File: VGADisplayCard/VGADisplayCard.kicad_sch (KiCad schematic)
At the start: 3 parts, among them J2 Bus_PCI_Express_x1

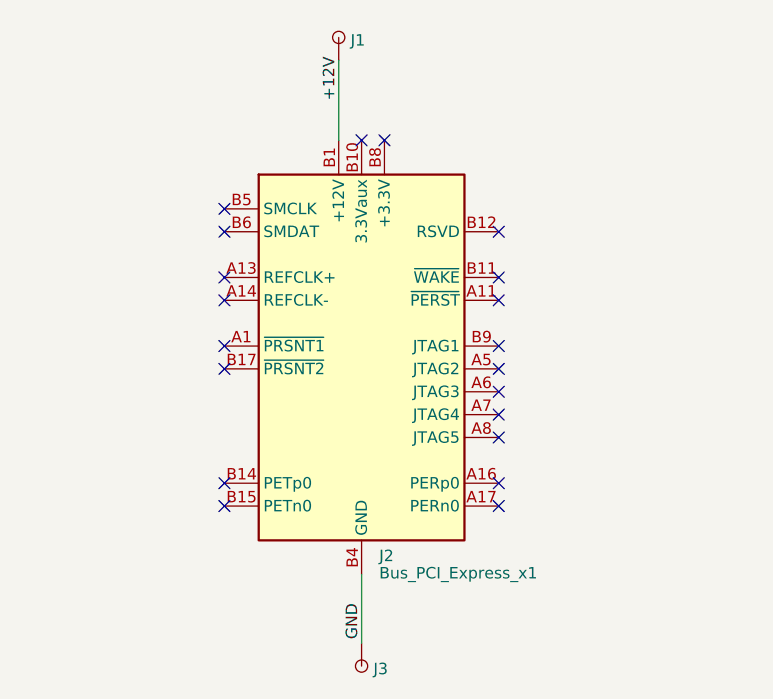
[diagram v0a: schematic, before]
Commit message: vga mount polish and 2.54mm mount (closes #37)
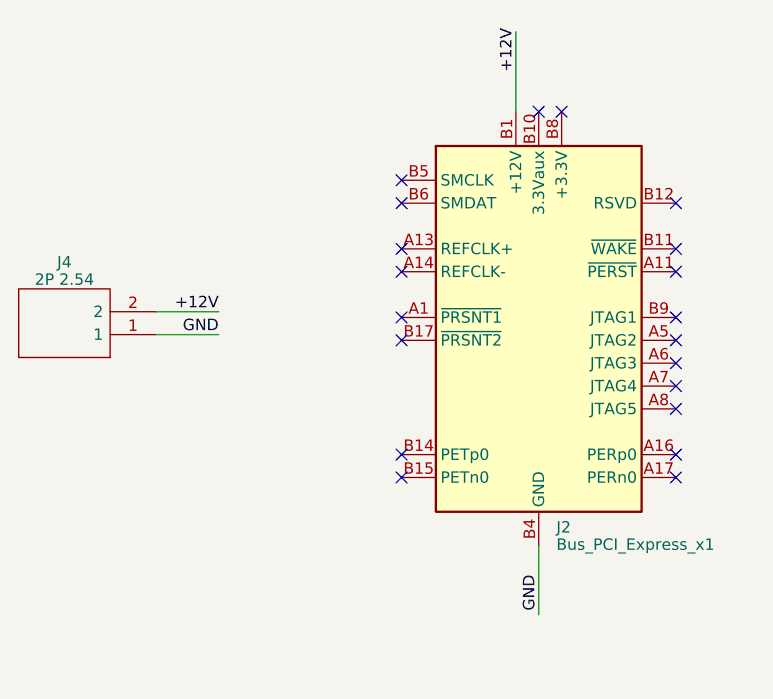
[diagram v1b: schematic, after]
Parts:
- removed J1, J3: ~, Oro Footprints:DebugPin, symbol Oro:DebugPin
- added J4: 2P 2.54, HDRV2W67P0X254_1X2_508X241X1082P, symbol SamacSys_Parts:10129378-902003BLF
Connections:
- net +12V: now also J4.2
- net GND: now also J4.1
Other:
- moved on the sheet: J2
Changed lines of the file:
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@@
   (title_block
     (title "PCIe.1x 12v Supply + VGA Mount")
-    (date "2023-06-09")
-    (rev "1")
+    (date "2023-07-02")
+    (rev "2")
     (company "Oro Operating System")
     (comment 1 "://oro.sh")
     (comment 2 "Joshua Lee Junon")
   )
-  (no_connect (at 158.115 106.045))
-  (no_connect (at 158.115 88.265))
-  (no_connect (at 158.115 108.585))
-  (no_connect (at 158.115 118.745))
-  (no_connect (at 142.875 78.105))
-  (no_connect (at 158.115 111.125))
-  (no_connect (at 158.115 95.885))
-  (no_connect (at 127.635 100.965))
-  (no_connect (at 127.635 116.205))
-  (no_connect (at 127.635 95.885))
-  (no_connect (at 158.115 116.205))
-  (no_connect (at 145.415 78.105))
-  (no_connect (at 158.115 100.965))
-  (no_connect (at 158.115 103.505))
-  (no_connect (at 127.635 103.505))
-  (no_connect (at 127.635 93.345))
-  (no_connect (at 127.635 88.265))
-  (no_connect (at 158.115 93.345))
-  (no_connect (at 127.635 118.745))
-  (no_connect (at 127.635 85.725))
-  (wire (pts (xy 142.875 126.365) (xy 142.875 133.985))
+  (no_connect (at 177.8 102.87))
+  (no_connect (at 177.8 85.09))
+  (no_connect (at 177.8 105.41))
+  (no_connect (at 177.8 115.57))
+  (no_connect (at 162.56 74.93))
+  (no_connect (at 177.8 107.95))
+  (no_connect (at 177.8 92.71))
+  (no_connect (at 147.32 97.79))
+  (no_connect (at 147.32 113.03))
+  (no_connect (at 147.32 92.71))
+  (no_connect (at 177.8 113.03))
+  (no_connect (at 165.1 74.93))
+  (no_connect (at 177.8 97.79))
+  (no_connect (at 177.8 100.33))
+  (no_connect (at 147.32 100.33))
+  (no_connect (at 147.32 90.17))
+  (no_connect (at 147.32 85.09))
+  (no_connect (at 177.8 90.17))
+  (no_connect (at 147.32 115.57))
+  (no_connect (at 147.32 82.55))
+  (wire (pts (xy 120.015 99.695) (xy 127 99.695))
     (stroke (width 0) (type default))
   )
-  (wire (pts (xy 140.335 69.215) (xy 140.335 78.105))
+  (wire (pts (xy 162.56 123.19) (xy 162.56 130.81))
     (stroke (width 0) (type default))
   )
-  (label "GND" (at 142.875 129.54 270) (fields_autoplaced)
+  (wire (pts (xy 120.015 97.155) (xy 127 97.155))
+    (stroke (width 0) (type default))
+  )
+  (wire (pts (xy 160.02 66.04) (xy 160.02 74.93))
+    (stroke (width 0) (type default))
+  )
+  (label "GND" (at 162.56 126.365 270) (fields_autoplaced)
     (effects (font (size 1.27 1.27)) (justify right bottom))
   )
-  (label "+12V" (at 140.335 73.66 90) (fields_autoplaced)
+  (label "+12V" (at 127 97.155 180) (fields_autoplaced)
+    (effects (font (size 1.27 1.27)) (justify right bottom))
+  )
+  (label "GND" (at 127 99.695 180) (fields_autoplaced)
+    (effects (font (size 1.27 1.27)) (justify right bottom))
+  )
+  (label "+12V" (at 160.02 70.485 90) (fields_autoplaced)
     (effects (font (size 1.27 1.27)) (justify left bottom))
   )
-  (symbol (lib_id "Connector:Bus_PCI_Express_x1") (at 142.875 103.505 0) (unit 1)
+  (symbol (lib_id "Connector:Bus_PCI_Express_x1") (at 162.56 100.33 0) (unit 1)
     (in_bom yes) (on_board yes) (dnp no) (fields_autoplaced)
-    (property "Reference" "J2" (at 144.8309 124.2775 0)
+    (property "Reference" "J2" (at 164.5159 121.1025 0)
       (effects (font (size 1.27 1.27)) (justify left))
     )
-    (property "Value" "Bus_PCI_Express_x1" (at 144.8309 126.1985 0)
+    (property "Value" "Bus_PCI_Express_x1" (at 164.5159 123.0235 0)
       (effects (font (size 1.27 1.27)) (justify left))
     )
-    (property "Footprint" "Connector_PCBEdge:BUS_PCIexpress_x1" (at 142.875 111.125 0)
+    (property "Footprint" "Connector_PCBEdge:BUS_PCIexpress_x1" (at 162.56 107.95 0)
       (effects (font (size 1.27 1.27)) hide)
     )
-    (property "Datasheet" "http://www.ritrontek.com/uploadfile/2016/1026/20161026105231124.pdf#page=63" (at 136.525 122.555 0)
+    (property "Datasheet" "http://www.ritrontek.com/uploadfile/2016/1026/20161026105231124.pdf#page=63" (at 156.21 119.38 0)
       (effects (font (size 1.27 1.27)) hide)
     )
@@
     )
   )
-  (symbol (lib_id "Oro:DebugPin") (at 140.335 69.215 90) (unit 1)
-    (in_bom no) (on_board yes) (dnp no) (fields_autoplaced)
-    (property "Reference" "J1" (at 141.6486 66.9918 90)
-      (effects (font (size 1.27 1.27)) (justify right))
+  (symbol (lib_id "SamacSys_Parts:10129378-902003BLF") (at 120.015 99.695 180) (unit 1)
+    (in_bom yes) (on_board yes) (dnp no) (fields_autoplaced)
+    (property "Reference" "J4" (at 109.855 91.6559 0)
+      (effects (font (size 1.27 1.27)))
     )
-    (property "Value" "~" (at 140.335 69.215 0)
-      (effects (font (size 1.27 1.27)) hide)
+    (property "Value" "2P 2.54" (at 109.855 93.5769 0)
+      (effects (font (size 1.27 1.27)))
     )
-    (property "Footprint" "Oro Footprints:DebugPin" (at 137.795 67.945 0)
-      (effects (font (size 1.27 1.27)) hide)
+    (property "Footprint" "HDRV2W67P0X254_1X2_508X241X1082P" (at 103.505 102.235 0)
+      (effects (font (size 1.27 1.27)) (justify left) hide)
     )
-    (property "Datasheet" "" (at 140.335 69.215 0)
-      (effects (font (size 1.27 1.27)) hide)
+    (property "Datasheet" "https://cdn.amphenol-cs.com/media/wysiwyg/files/drawing/10129378.pdf" (at 103.505 99.695 0)
+      (effects (font (size 1.27 1.27)) (justify left) hide)
     )
-    (property "Sim.Enable" "0" (at 137.795 55.245 0)
-      (effects (font (size 1.27 1.27)) hide)
+    (property "Description" "EconoStik 2.54mm, Board to Board Connector, Unshrouded Verticl Header, Through Hole, Single Row, 2 Positions, 2.54 mm (0.100in) Pitch." (at 103.505 97.155 0)
+      (effects (font (size 1.27 1.27)) (justify left) hide)
+    )
+    (property "Height" "10.82" (at 103.505 94.615 0)
+      (effects (font (size 1.27 1.27)) (justify left) hide)
+    )
+    (property "Manufacturer_Name" "Amphenol Communication Solutions" (at 103.505 92.075 0)
+      (effects (font (size 1.27 1.27)) (justify left) hide)
+    )
+    (property "Manufacturer_Part_Number" "10129378-902003BLF" (at 103.505 89.535 0)
+      (effects (font (size 1.27 1.27)) (justify left) hide)
+    )
+    (property "Mouser Part Number" "649-1012937890203BLF" (at 103.505 86.995 0)
+      (effects (font (size 1.27 1.27)) (justify left) hide)
+    )
+    (property "Mouser Price/Stock" "https://www.mouser.co.uk/ProductDetail/Amphenol-FCI/10129378-902003BLF?qs=0lQeLiL1qyZU%252BgRaQ8FKPg%3D%3D" (at 103.505 84.455 0)
+      (effects (font (size 1.27 1.27)) (justify left) hide)
+    )
+    (property "Arrow Part Number" "" (at 103.505 81.915 0)
+      (effects (font (size 1.27 1.27)) (justify left) hide)
+    )
+    (property "Arrow Price/Stock" "" (at 103.505 79.375 0)
+      (effects (font (size 1.27 1.27)) (justify left) hide)
     )
     (pin "1")
+    (pin "2")
     (instances
       (project "VGADisplayCard"
         (path "/e0904bb7-cbd8-452a-833e-2efbcf63295e"
-          (reference "J1") (unit 1)
+          (reference "J4") (unit 1)
         )
       )
-    )
-  )
-  (symbol (lib_id "Oro:DebugPin") (at 142.875 133.985 270) (unit 1)
-    (in_bom no) (on_board yes) (dnp no) (fields_autoplaced)
-    (property "Reference" "J3" (at 144.1886 136.8418 90)
-      (effects (font (size 1.27 1.27)) (justify left))
-    )
-    (property "Value" "~" (at 142.875 133.985 0)
-      (effects (font (size 1.27 1.27)) hide)
-    )
-    (property "Footprint" "Oro Footprints:DebugPin" (at 145.415 135.255 0)
-      (effects (font (size 1.27 1.27)) hide)
-    )
-    (property "Datasheet" "" (at 142.875 133.985 0)
-      (effects (font (size 1.27 1.27)) hide)
-    )
-    (property "Sim.Enable" "0" (at 145.415 147.955 0)
-      (effects (font (size 1.27 1.27)) hide)
-    )
-    (pin "1")
-    (instances
-      (project "VGADisplayCard"
-        (path "/e0904bb7-cbd8-452a-833e-2efbcf63295e"
-          (reference "J3") (unit 1)
+      (project "OroLink"
+        (path "/e89dcd22-1250-4a5b-b778-1c95a0dd623d/259c9346-7ad9-40c3-9e14-9b19afc78ddf"
+          (reference "J9") (unit 1)
         )
       )
